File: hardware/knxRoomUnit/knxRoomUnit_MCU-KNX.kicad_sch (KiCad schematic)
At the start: 28 parts, among them J1 PROG, J2 KNX, Q1 S8050, Q2 S8050, SW1 RESET, SW2 KNX, SW3 DW, SW4 OK, SW5 UP, U1 ESP32-WROOM-32

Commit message: Updated HW design
Flipped P1 to match display's pinout
Changed 0201 resistors to 0603
Added R12 to section 3V3 to display
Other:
- company: (none) -> MP
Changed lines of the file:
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@@
   (title_block
     (title "knxRoomUnit")
-    (date "2023-08-22")
-    (rev "r1d0")
+    (date "2024-01-21")
+    (rev "r1d1")
+    (company "MP")
   )
   (junction (at 54.61 34.29) (diameter 0) (color 0 0 0 0)

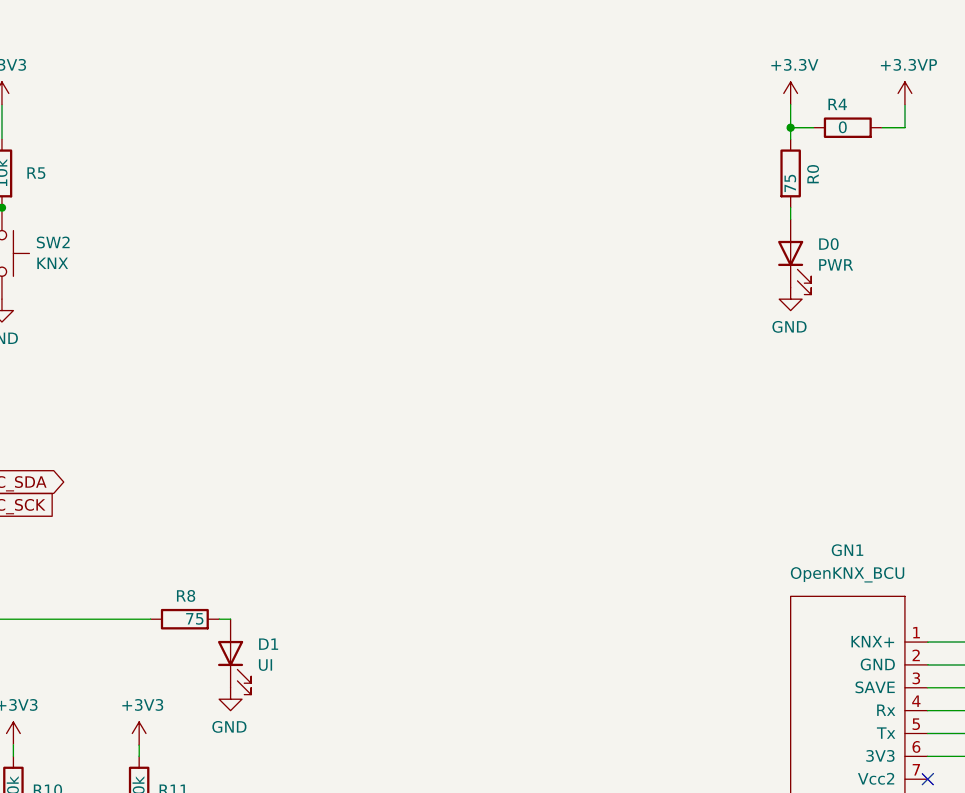
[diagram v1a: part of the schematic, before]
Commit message: Updated HW design
Changed R0/R8 to 470R
PCB routing and DRC
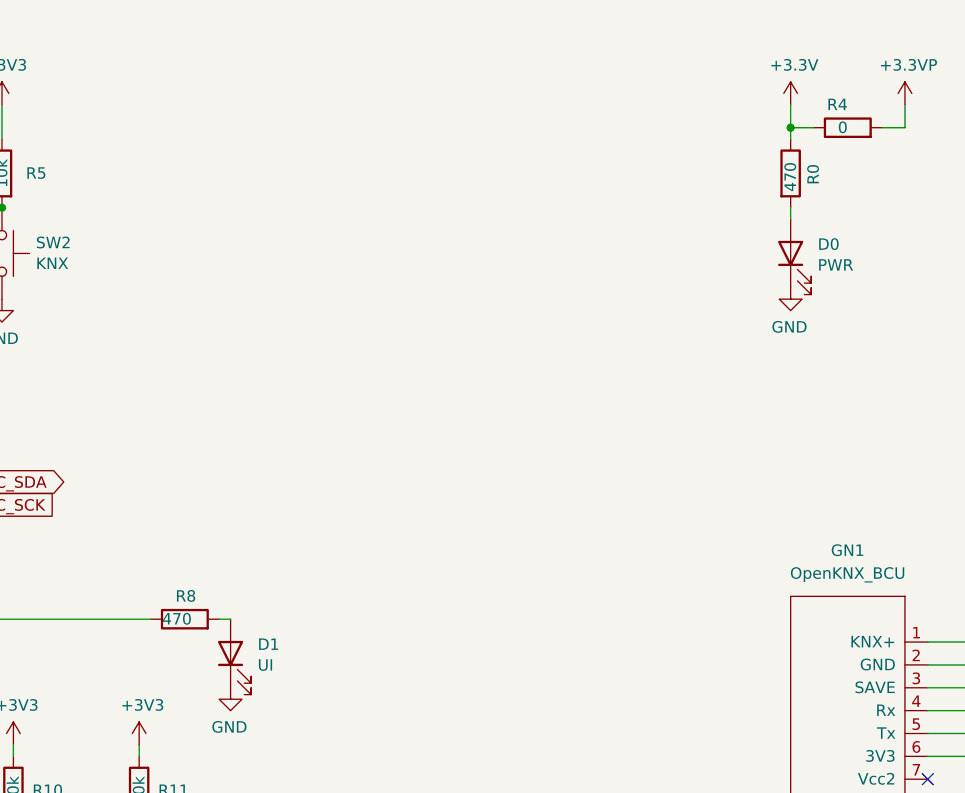
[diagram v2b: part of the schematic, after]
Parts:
- R0, R8: value 75 -> 470; LCSC Part # C21189 -> C23179; PartNumber 0603WAF0000T5E -> 0603WAF4700T5E
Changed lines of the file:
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@@
       (effects (font (size 1.27 1.27)) (justify left))
     )
-    (property "Value" "75" (at 163.83 83.82 90)
+    (property "Value" "470" (at 161.29 83.82 90)
       (effects (font (size 1.27 1.27)) (justify right))
     )
@@
       (effects (font (size 1.27 1.27)) hide)
     )
-    (property "Datasheet" "https://datasheet.lcsc.com/lcsc/2206010130_UNI-ROYAL-Uniroyal-Elec-0603WAF0000T5E_C21189.pdf" (at 163.83 83.82 0)
-      (effects (font (size 1.27 1.27)) hide)
-    )
-    (property "LCSC Part #" "C21189" (at 163.83 83.82 0)
+    (property "Datasheet" "https://datasheet.lcsc.com/lcsc/2206010116_UNI-ROYAL-Uniroyal-Elec-0603WAF4700T5E_C23179.pdf" (at 163.83 83.82 0)
+      (effects (font (size 1.27 1.27)) hide)
+    )
+    (property "LCSC Part #" "C23179" (at 163.83 83.82 0)
       (effects (font (size 1.27 1.27)) hide)
     )
@@
       (effects (font (size 1.27 1.27)) hide)
     )
-    (property "PartNumber" "0603WAF0000T5E" (at 163.83 83.82 0)
+    (property "PartNumber" "0603WAF4700T5E" (at 163.83 83.82 0)
       (effects (font (size 1.27 1.27)) hide)
     )
@@
       (effects (font (size 1.27 1.27)) (justify left))
     )
-    (property "Value" "75" (at 231.14 34.29 90)
+    (property "Value" "470" (at 231.14 33.02 90)
       (effects (font (size 1.27 1.27)) (justify right))
     )
@@
       (effects (font (size 1.27 1.27)) hide)
     )
-    (property "Datasheet" "https://datasheet.lcsc.com/lcsc/2206010130_UNI-ROYAL-Uniroyal-Elec-0603WAF0000T5E_C21189.pdf" (at 231.14 34.29 0)
-      (effects (font (size 1.27 1.27)) hide)
-    )
-    (property "LCSC Part #" "C21189" (at 231.14 34.29 0)
+    (property "Datasheet" "https://datasheet.lcsc.com/lcsc/2206010116_UNI-ROYAL-Uniroyal-Elec-0603WAF4700T5E_C23179.pdf" (at 231.14 34.29 0)
+      (effects (font (size 1.27 1.27)) hide)
+    )
+    (property "LCSC Part #" "C23179" (at 231.14 34.29 0)
       (effects (font (size 1.27 1.27)) hide)
     )
@@
       (effects (font (size 1.27 1.27)) hide)
     )
-    (property "PartNumber" "0603WAF0000T5E" (at 231.14 34.29 0)
-      (effects (font (size 1.27 1.27)) hide)
-    )
+    (property "PartNumber" "0603WAF4700T5E" (at 231.14 34.29 0)
+      (effects (font (size 1.27 1.27)) hide)
+    )
